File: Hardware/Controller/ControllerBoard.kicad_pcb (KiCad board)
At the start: 2 copper layers, 25 x 140 mm, 12 parts, among them J1 Conn_01x08_MountingPin, J2 USB4715-GF-A_REVA, X1 CON_JST_PH_2PIN_MTPH2

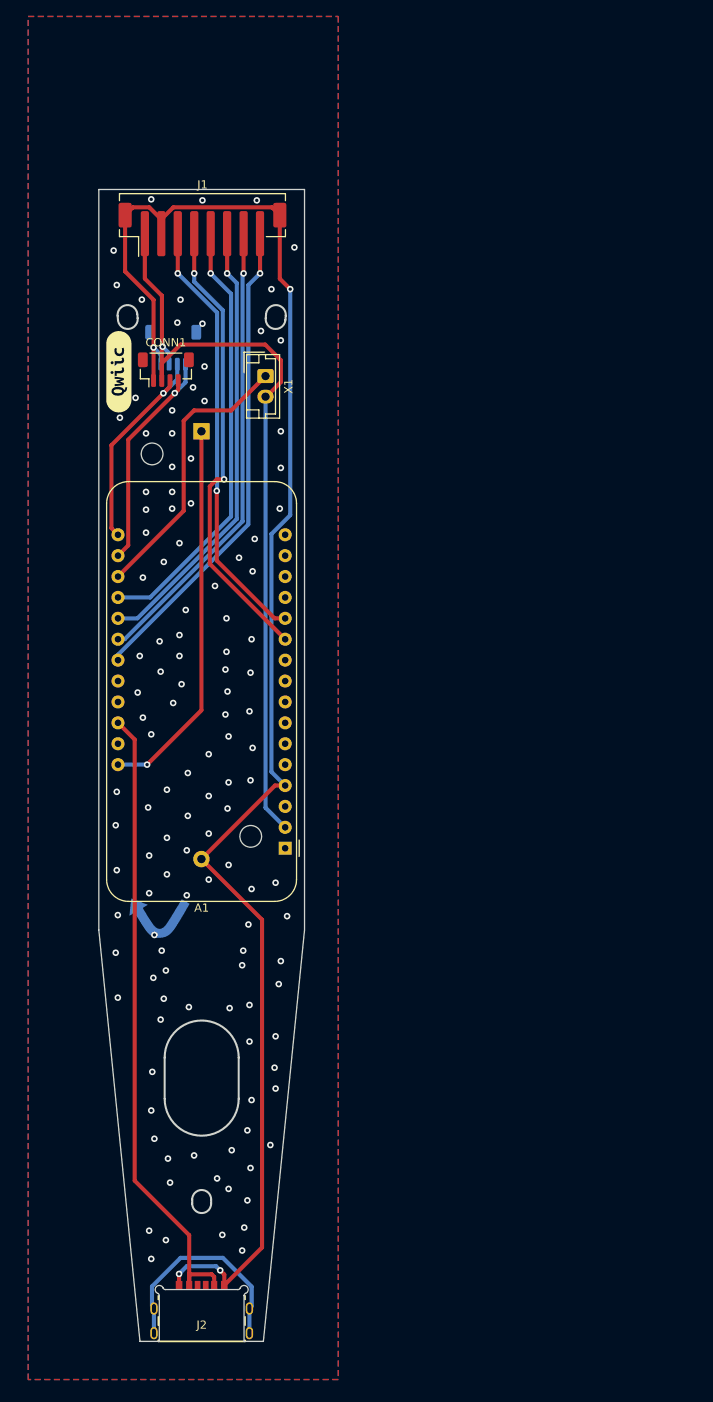
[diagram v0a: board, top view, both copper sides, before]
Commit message: battery move and horizontal connector
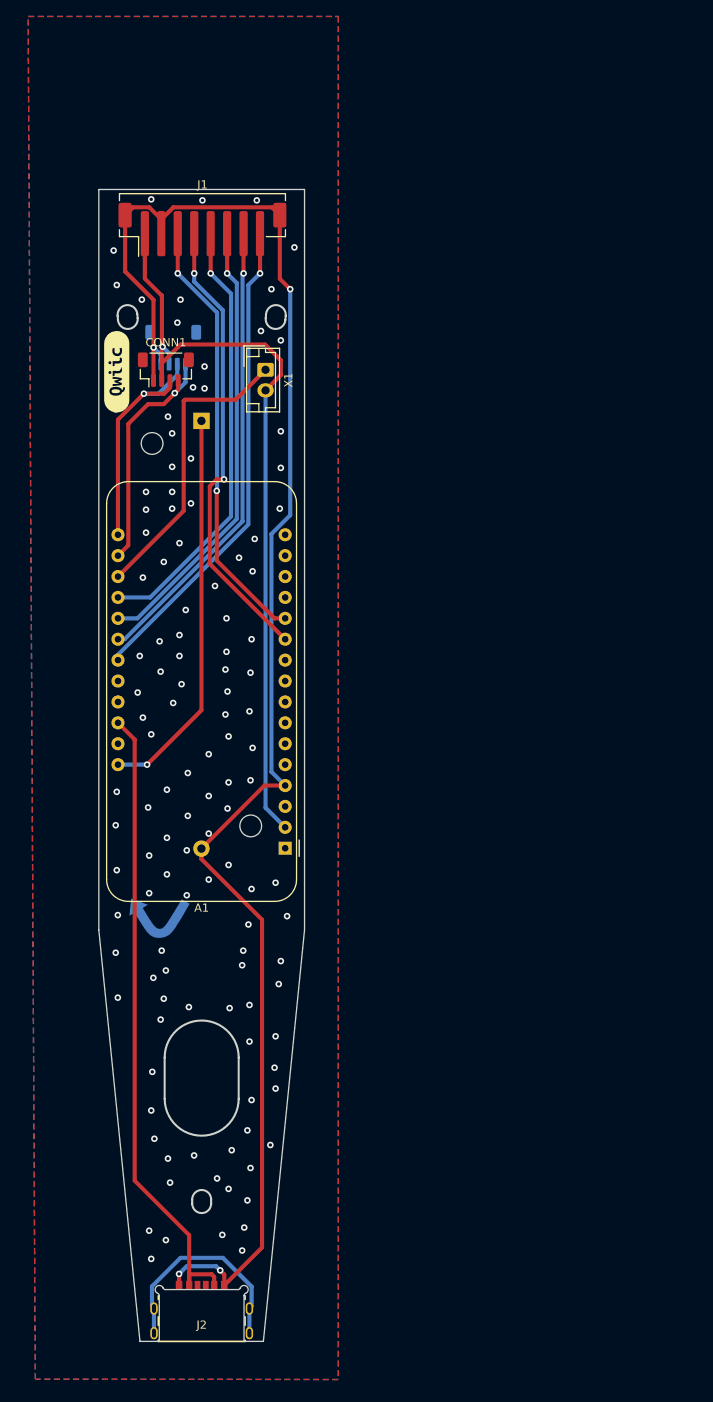
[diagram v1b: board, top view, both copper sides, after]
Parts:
- moved BT1 1.27 mm to (110.6, 63.1)
- moved X1 0.76 mm to (118.4, 56.9)
- moved kibuzzard-63988507 0.25 mm to (100.3, 57.1) (x2)
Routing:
- net Net-(A1-Pad17): track 26.3 -> 29.1 mm
- net Net-(A1-Pad19): track 34.4 -> 36.2 mm
- net Net-(A1-Pad28): track 46.8 -> 48.1 mm
- net Net-(A1-Pad18): track 28.4 -> 29.5 mm
- net GND: track 197.6 -> 198.4 mm, vias 131 -> 127

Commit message: LAtching circuit for controller board + minors
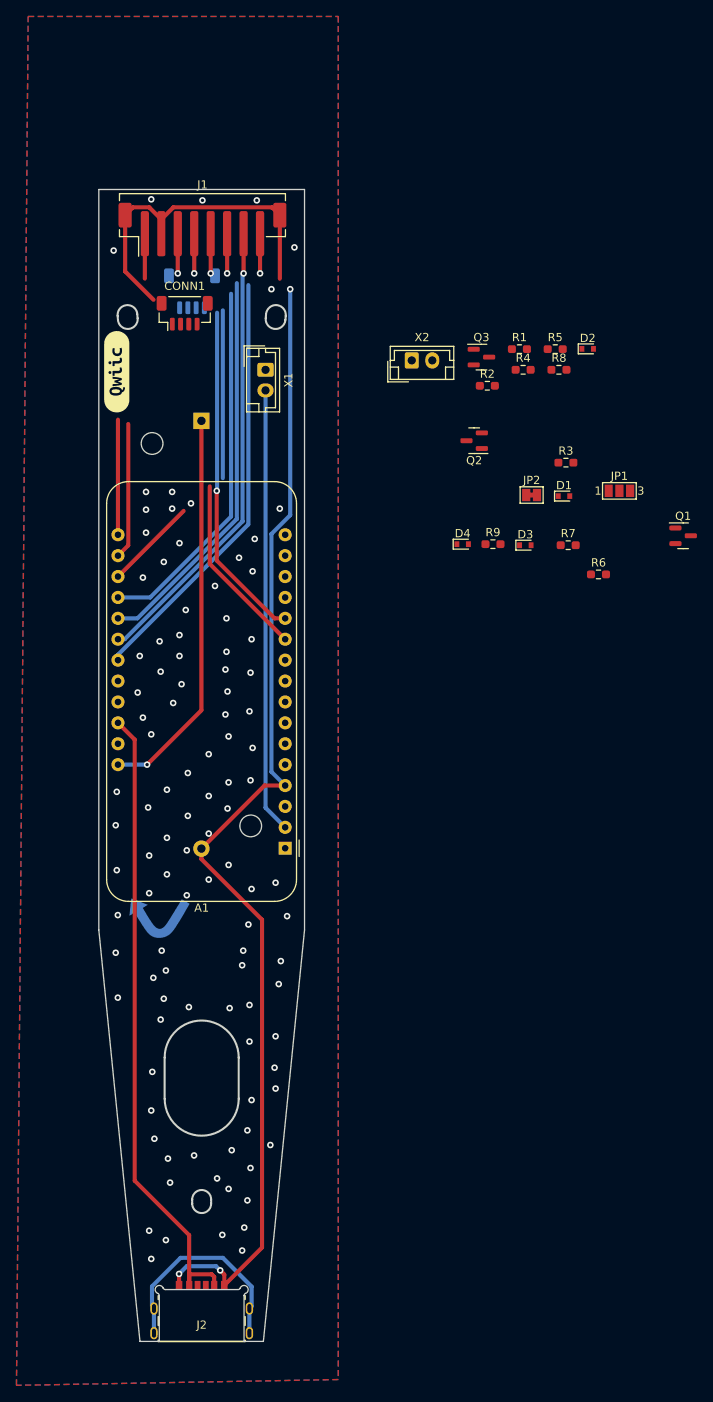
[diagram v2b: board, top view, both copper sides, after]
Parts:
- added D1: BAS516, Diode_SMD:D_SOD-523, F.Cu at (154.7, 72.3)
- added D2: BAS516, Diode_SMD:D_SOD-523, F.Cu at (157.6, 54.4)
- added D3: BAS516, Diode_SMD:D_SOD-523, F.Cu at (150.0, 78.2)
- added D4: BAS516, Diode_SMD:D_SOD-523, F.Cu at (142.4, 78.1)
- added JP1: SolderJumper_3_Open, Jumper:SolderJumper-3_P1.3mm_Open_Pad1.0x1.5mm_NumberLabels, F.Cu at (161.4, 71.6)
- added JP2: SolderJumper_2_Bridged, Jumper:SolderJumper-2_P1.3mm_Bridged_Pad1.0x1.5mm, F.Cu at (150.7, 72.1)
- added Q1: BC818, Package_TO_SOT_SMD:SOT-23, F.Cu at (169.2, 77.1)
- added Q2: AO3401A, Package_TO_SOT_SMD:SOT-23, F.Cu at (143.8, 65.5)
- added Q3: BC818, Package_TO_SOT_SMD:SOT-23, F.Cu at (144.6, 55.4)
- added R1: 5.1k, Resistor_SMD:R_0603_1608Metric_Pad0.98x0.95mm_HandSolder, F.Cu at (149.3, 54.4)
- added R2: 5.1k, Resistor_SMD:R_0603_1608Metric_Pad0.98x0.95mm_HandSolder, F.Cu at (145.4, 58.9)
- added R3: 1k, Resistor_SMD:R_0603_1608Metric_Pad0.98x0.95mm_HandSolder, F.Cu at (154.9, 68.2)
- added R4: 100k, Resistor_SMD:R_0603_1608Metric_Pad0.98x0.95mm_HandSolder, F.Cu at (149.7, 56.9)
- added R5: 10k, Resistor_SMD:R_0603_1608Metric_Pad0.98x0.95mm_HandSolder, F.Cu at (153.6, 54.4)
- added R6: 220k, Resistor_SMD:R_0603_1608Metric_Pad0.98x0.95mm_HandSolder, F.Cu at (158.9, 81.8)
- added R7: 10k, Resistor_SMD:R_0603_1608Metric_Pad0.98x0.95mm_HandSolder, F.Cu at (155.2, 78.2)
- added R8: 100k, Resistor_SMD:R_0603_1608Metric_Pad0.98x0.95mm_HandSolder, F.Cu at (154.1, 56.9)
- added R9: 220, Resistor_SMD:R_0603_1608Metric_Pad0.98x0.95mm_HandSolder, F.Cu at (146.1, 78.1)
- added X2: CON_JST_PH_2PIN_MTPH2, Connector_JST:JST_EH_B2B-EH-A_1x02_P2.50mm_Vertical, F.Cu at (136.2, 55.8)
- moved CONN1 7.23 mm to (108.6, 50.0)
- moved CONN2 7.23 mm to (109.5, 47.4)
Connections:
- net Net-(A1-Pad26) renamed USB_pwr
- A1 pad 19: Net-(A1-Pad19) -> unconnected-(A1-Pad19)
- A1 pad 24: unconnected-(A1-Pad24) -> KeepAlive
- A1 pad 25: unconnected-(A1-Pad25) -> Trigger
- A1 pad 28: Net-(A1-Pad28) -> power for the esp32
- BT1 pad 1: Net-(A1-Pad28) -> Net-(BT1-Pad1)
- J2 pad A5: unconnected-(J2-PadA5) -> Net-(J2-PadA5)
- J2 pad B5: unconnected-(J2-PadB5) -> Net-(J2-PadB5)
- X1 pad 1: Net-(A1-Pad19) -> Net-(JP1-Pad2)
- X1 pad 2: 3.3V -> Net-(BT1-Pad1)
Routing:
- net power for the esp32: track 0.00 -> 48.1 mm, vias 0 -> 1
- net Net-(A1-Pad28): track 48.1 -> 0.00 mm, vias 1 -> 0
- net 3.3V: track 98.1 -> 59.6 mm, vias 1 -> 0
- net Net-(A1-Pad19): track 36.2 -> 0.00 mm
- net Net-(A1-Pad17): track 29.1 -> 14.0 mm, vias 1 -> 0
- net GND: track 198.4 -> 184.4 mm, vias 127 -> 108
- net Net-(A1-Pad18): track 29.5 -> 16.5 mm, vias 1 -> 0
- net unconnected-(A1-Pad19): track 0.00 -> 11.3 mm
- net Net-(A1-Pad11): track 55.8 -> 47.6 mm, vias 2 -> 1
- net Net-(A1-Pad12): track 52.9 -> 46.1 mm
- net Net-(A1-Pad20): track 53.2 -> 49.7 mm
- net Net-(A1-Pad23): track 59.0 -> 57.0 mm
- net Net-(A1-Pad21): track 54.6 -> 52.9 mm

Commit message: Reroutes tracks to add funtion of latching circuit
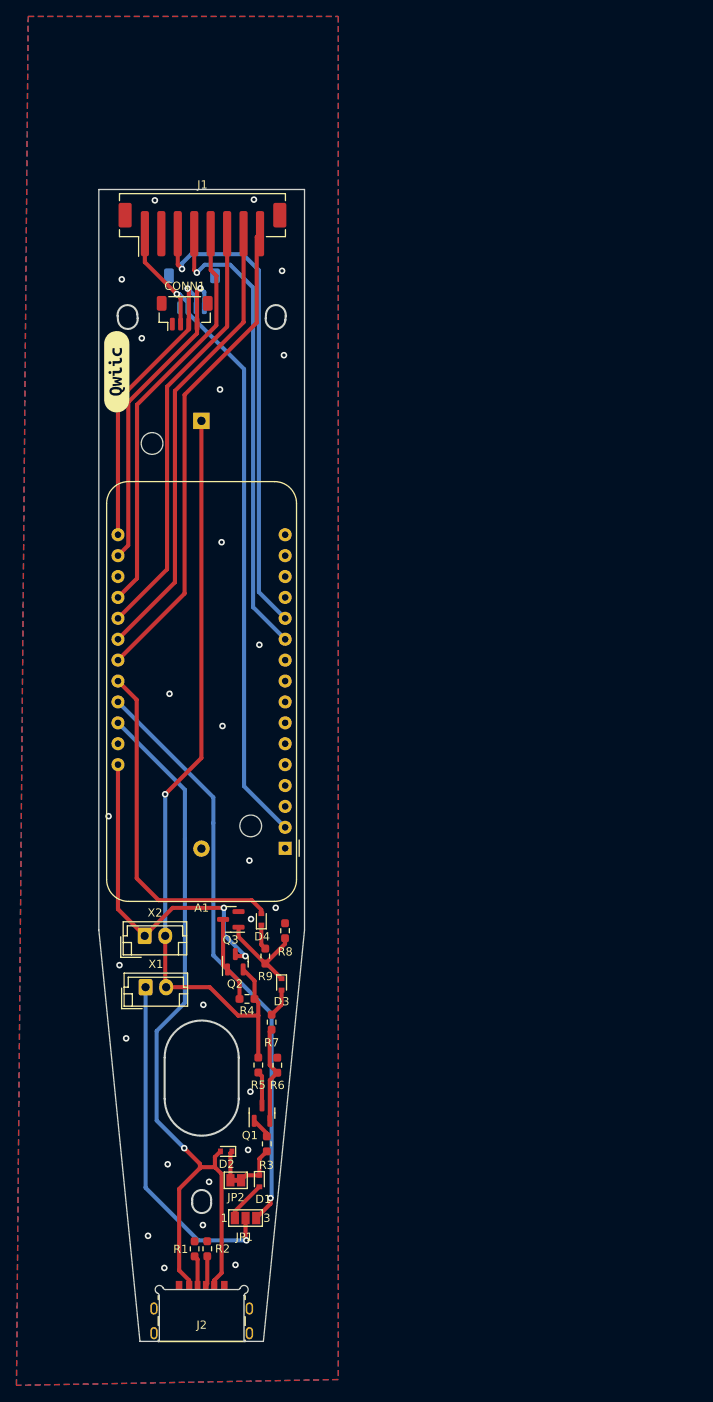
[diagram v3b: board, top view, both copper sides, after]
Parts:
- moved R1 116.3 mm to (109.8, 163.8), turned to 90 degrees
- moved R2 110.3 mm to (111.3, 163.7), turned to -90 degrees
- moved D2 107.0 mm to (113.6, 151.9), turned to 180 degrees
- moved JP1 99.4 mm to (116.0, 160.0)
- moved R5 94.2 mm to (117.5, 141.4), turned to 90 degrees
- moved D1 91.1 mm to (117.7, 155.5), turned to -90 degrees
- moved JP2 90.7 mm to (114.8, 155.4)
- moved R3 90.4 mm to (118.6, 151.0), turned to 90 degrees
- moved Q1 86.8 mm to (118.0, 147.3), turned to 90 degrees
- moved R4 83.5 mm to (116.2, 133.4), turned to 180 degrees
- moved X2 77.1 mm to (103.7, 125.7)
- moved X1 76.4 mm to (103.8, 131.9), turned to 0 degrees
- moved R8 75.9 mm to (120.8, 125.1), turned to -90 degrees
- moved Q3 74.8 mm to (114.2, 123.7), turned to 180 degrees
- moved R6 71.3 mm to (119.8, 141.4), turned to -90 degrees
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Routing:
- net GND: track 184.4 -> 0.00 mm, vias 108 -> 26
- net Net-(BT1-Pad1): track 0.00 -> 94.8 mm, vias 0 -> 1
- net Trigger: track 0.00 -> 71.2 mm, vias 0 -> 1
- net KeepAlive: track 0.00 -> 42.1 mm
- net Net-(JP1-Pad2): track 0.00 -> 42.0 mm, vias 0 -> 1
- net Net-(J2-PadS1): track 26.6 -> 0.00 mm
- net 3.3V: track 59.6 -> 83.2 mm, vias 0 -> 1
- net Net-(A1-Pad18): track 16.5 -> 39.2 mm, vias 0 -> 1
- net Net-(A1-Pad17): track 14.0 -> 36.3 mm, vias 0 -> 1
- net USB_pwr: track 77.5 -> 96.0 mm, vias 0 -> 1
- net Net-(A1-Pad12): track 46.1 -> 59.4 mm, vias 2 -> 1
- net Net-(D3-Pad1): track 0.00 -> 12.6 mm
- net Net-(Q1-Pad2): track 0.00 -> 11.9 mm
- net unconnected-(A1-Pad19): track 11.3 -> 0.00 mm
- net Net-(Q2-Pad1): track 0.00 -> 10.5 mm
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
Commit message: Scanner & Controller Version 1.0
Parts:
- moved PlasticScannerLogo 12.2 mm to (117.7, 121.4)
- moved OSH logo 11.1 mm to (104.8, 120.8)
- moved kibuzzard-63988507 10.0 mm to (109.9, 54.0), turned to 180 degrees
- moved kibuzzard-63988507 8.68 mm to (108.6, 54.5), turned to 180 degrees
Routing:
- net GND: track 0.00 -> 5.88 mm
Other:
- board text added: "MCU board - Version 1.0"
- board text removed: "MCU board - Version 0.2"
